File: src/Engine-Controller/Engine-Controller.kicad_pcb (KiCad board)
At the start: 4 copper layers, 116.8 x 56.7 mm, 123 parts, among them J1 Jumper_NO, J2 Jumper_NO, P1 EJ508A, P10 282837-2, P11 282837-2, P17 0530470410, P18 PPTC041LFBN-RC, P2 282837-6, P3 3220-20-0200-00, P4 Micro_SD_Card, P5 USB, P6 140-504-415-000, P7 647676-2, P8 20021511-00026T4LF, P9 5015680807, Q1 QS5U17TR, U1 STM32H750VBTx, U10 LMS8117AMP-3.3_NOPB, U11 TS391IYLT, U12 MAX4617EUE+T, U13 MAX4617EUE+T, U14 MCP96L01T-E_MX, U15 AD623ARZ-R7, U2 LM22672MRE-5.0_NOPB, U3 LMS8117AMP-3.3_NOPB, U4 SST25VF040B-50-4I-S2AE-T, U5 CP2102-GMR(QFN28), U6 TPS2115APWR, U8 AD623ARZ-R7, Y1 ECS-240-18-33-JGN-TR

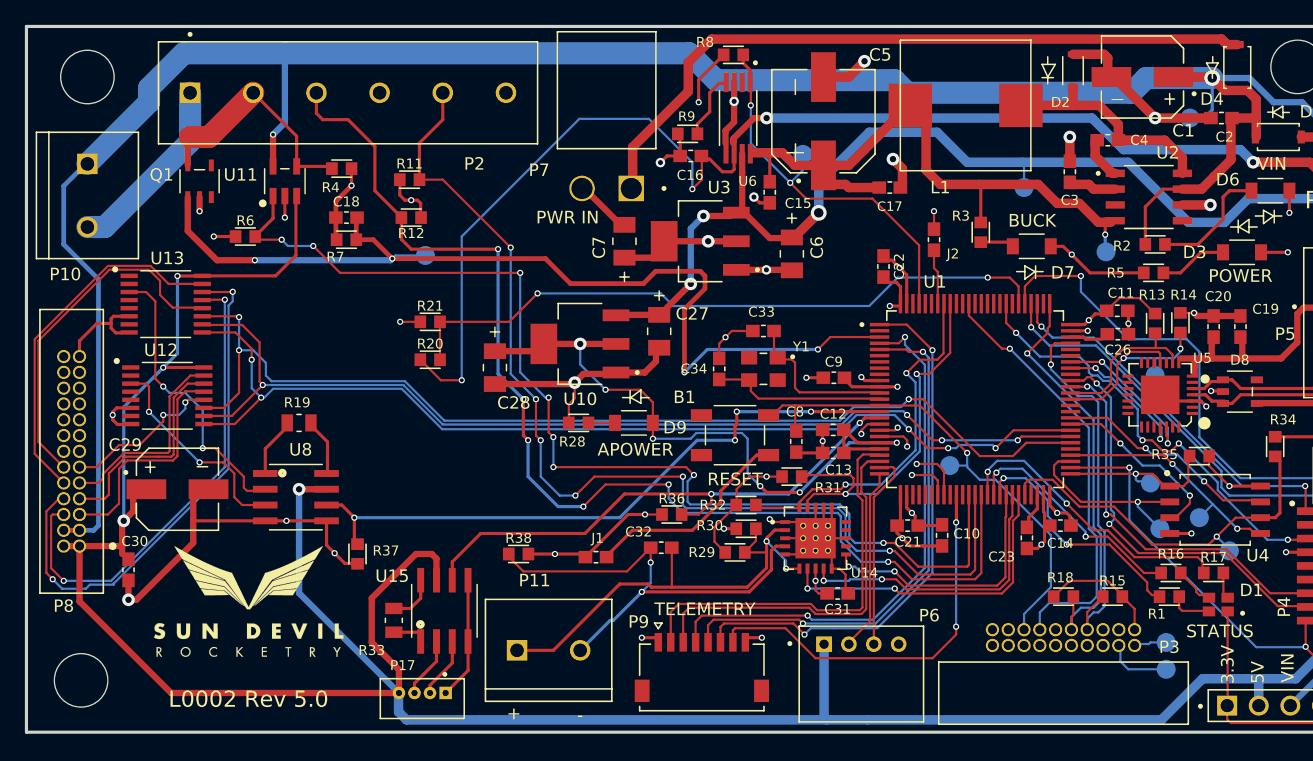
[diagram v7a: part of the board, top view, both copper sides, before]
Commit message: fixed broken paths to step files and placed all 5.1 components on board
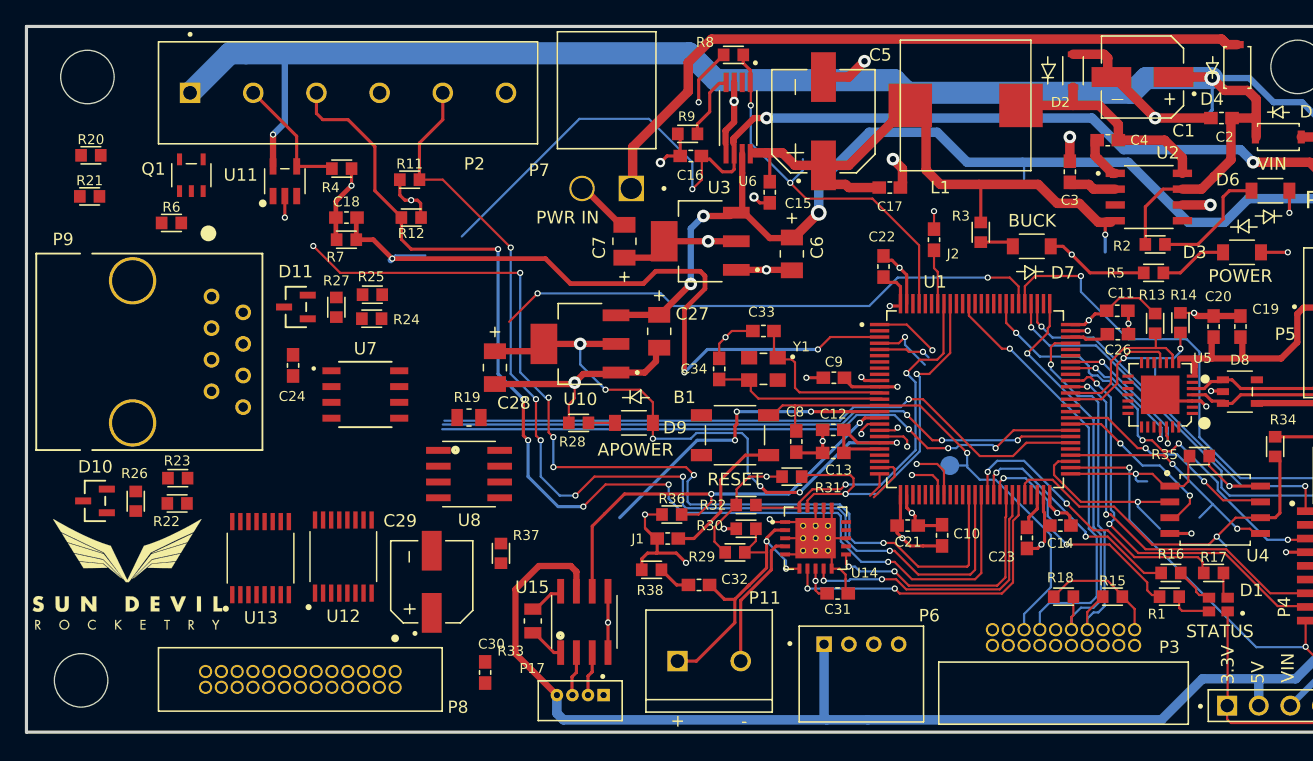
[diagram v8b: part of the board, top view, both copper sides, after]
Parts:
- removed P10: 282837-2, Engine-Controller:282837-2
- removed TP10, TP11, TP12, TP13, TP6, TP7, TP8, TP9: TP, Engine-Controller:TP
- removed TP2: TPVIN, Engine-Controller:TP
- removed TP3: TPGND, Engine-Controller:TP
- removed TP4: TP5V, Engine-Controller:TP
- removed TP5: 3.3V, Engine-Controller:TP
- added C24: 0.1uF, Engine-Controller:CAP_0603, F.Cu at (107.8, 122.9)
- added D10: SMBJ36CA-13-F, Engine-Controller:CDSOT23-SM712, F.Cu at (91.9, 133.8)
- added D11: SMBJ36CA-13-F, Engine-Controller:CDSOT23-SM712, F.Cu at (108.0, 118.2)
- added R22: 10, Engine-Controller:RES_0603, F.Cu at (98.5, 134.0)
- added R23: 10, Engine-Controller:RES_0603, F.Cu at (98.5, 132.0)
- added R24: 10, Engine-Controller:RES_0603, F.Cu at (114.1, 119.2)
- added R25: 10, Engine-Controller:RES_0603, F.Cu at (114.2, 117.2)
- added R26: 100, Engine-Controller:RES_0603, F.Cu at (95.1, 133.8)
- added R27: 100, Engine-Controller:RES_0603, F.Cu at (111.3, 118.2)
- added U7: SN65HVD71DR, Engine-Controller:SN65HVD71DR, F.Cu at (113.6, 125.2)
- B1: value PTS647SM38SMTR2LFS -> SW_PTS647SM38SMTR2LFS_CNK
- D2: value RB160VAM-60TR -> DIO_RB160VAM_ROM
- D4, D5: value SM5819PL-TP -> SOD-123FL_MCC
- D8: value SP0504BAHTG -> SP0504BAHTG_LTF
- P9: value 5015680807 -> 54602-908LF; footprint Engine-Controller:5015680807 -> Engine-Controller:54602-908LF
- Q1: value QS5U17TR -> TRANS_QS5K_ROM
- R1: value 68 -> 82
- U11: value TS391IYLT -> SOT23-5_STM
- U14: value MCP96L01T-E_MX -> QFN65P500X500X100-21N_MCP96RL00T-E/MX
- U15, U8: value AD623ARZ-R7 -> R_8_ADI
- U2: value LM22672MRE-5.0_NOPB -> VREG_LM5017MR/NOPB
- U4: value SST25VF040B-50-4I-S2AE-T -> SOIC8_S2A_SST_MCH
- moved P9 49.8 mm to (101.2, 117.4), turned to -90 degrees
- moved R20 31.8 mm to (91.5, 106.0)
- moved C30 29.8 mm to (123.2, 147.6)
- moved R21 29.2 mm to (91.4, 109.3)
- moved P8 26.0 mm to (108.4, 148.2), turned to 180 degrees
- moved U13 21.8 mm to (105.2, 138.4), turned to 90 degrees
- moved C29 21.8 mm to (118.9, 140.3), turned to 90 degrees
- moved U12 19.2 mm to (111.8, 138.3), turned to 90 degrees
- moved U8 14.0 mm to (121.9, 131.6)
- moved R19 13.7 mm to (121.9, 127.1)
- moved P11 12.9 mm to (141.2, 146.7)
- moved P17 12.7 mm to (130.9, 149.4)
- moved R37 11.5 mm to (124.5, 138.0)
- moved U15 11.3 mm to (131.2, 143.5)
- moved R33 11.2 mm to (127.1, 143.5)
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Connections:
- P2 pad 1: Net-(P10-6) -> VIN
- P6 pad 1: 5V -> Earth
- P6 pad 2: ValveCtrl_TX -> ValveCtrl_RX
- P6 pad 3: ValveCtrl_RX -> ValveCtrl_TX
- P6 pad 4: Earth -> 5V
- P9 pad 1: 3.3V -> Z
- P9 pad 2: W_TX -> Y
- P9 pad 3: W_RX -> unconnected-(P9-Pad3)
- P9 pad 4: W_MISO -> unconnected-(P9-Pad4)
- P9 pad 5: W_MOSI -> unconnected-(P9-Pad5)
- P9 pad 6: W_SCK -> unconnected-(P9-Pad6)
- P9 pad 7: W_SS -> B
- P9 pad 8: Earth -> A
- U1 pad 1: W_SCK -> unconnected-(U1-PE2-Pad1)
- U1 pad 22: W_TX -> RS485_TX
- U1 pad 23: W_RX -> RS485_RX
- U1 pad 35: W_SS -> unconnected-(U1-PB1-Pad35)
- U1 pad 4: W_MISO -> unconnected-(U1-PE5-Pad4)
- U1 pad 5: W_MOSI -> unconnected-(U1-PE6-Pad5)
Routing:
- net 5V: track 336.4 -> 220.1 mm, vias 7 -> 3
- net Earth: track 251.5 -> 196.8 mm, vias 40 -> 34
- net PT5+: track 66.4 -> 12.5 mm
- net PT6+: track 70.0 -> 19.0 mm
- net VIN: track 245.6 -> 200.0 mm
- net W_SCK: track 43.8 -> 0.00 mm, vias 2 -> 0
- net W_MISO: track 43.6 -> 0.00 mm, vias 2 -> 0
- net PT2-: track 42.8 -> 0.00 mm, vias 2 -> 0
- net W_MOSI: track 42.5 -> 0.00 mm, vias 2 -> 0
- net PT7+: track 77.7 -> 39.2 mm
- net PT1-: track 38.3 -> 0.00 mm, vias 2 -> 0
- net PT8+: track 78.0 -> 40.2 mm
- net W_TX: track 32.8 -> 0.00 mm
- net W_SS: track 32.0 -> 0.00 mm, vias 2 -> 0
- net PT_MUX_A: track 85.3 -> 53.4 mm, vias 3 -> 1
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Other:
- board text added: "Cred. Colton Acosta 2019-2023 OG Liquids Avionics"
- board text added: "L0002 Liquid Engine Controller Rev 5.1 Sun Devil Rocketry Avionics"
- board text removed: "L0002 Rev 5.0"
- board text removed: "SWITCH"
- board text removed: "TELEMETRY"
